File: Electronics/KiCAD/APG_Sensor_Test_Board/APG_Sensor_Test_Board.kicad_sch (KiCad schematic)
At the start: 0 parts

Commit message: Main Schematic Complete
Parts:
- added J2: Conn_01x02, symbol Connector_Generic:Conn_01x02
- added J3, J6: Conn_01x05, symbol Connector_Generic:Conn_01x05
- added J5: Conn_01x03, symbol Connector_Generic:Conn_01x03
- added R17, R18: 10k, symbol Device:R
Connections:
- net Baro/SCLK: now also R17.2
- net ESP32/IO1: now also J3.1 (Pin_1)
- net ESP32/IO10: now also J3.5 (Pin_5)
- net ESP32/IO18: now also J6.1 (Pin_1)
- net ESP32/IO2: now also J3.2 (Pin_2)
- net ESP32/IO38: now also J6.2 (Pin_2)
- net ESP32/IO39: now also J6.3 (Pin_3)
- net ESP32/IO40: now also J6.4 (Pin_4)
- net ESP32/IO41: now also J6.5 (Pin_5)
- net ESP32/IO42: now also J5.1 (Pin_1)
- net ESP32/IO8: now also J3.3 (Pin_3)
- net ESP32/IO9: now also J3.4 (Pin_4)
- net ESP32/RX: now also J5.2 (Pin_2)
- net ESP32/TX: now also J5.3 (Pin_3)
- new net +3V3: R17.1, R18.1
- new net ADC1: J2.2 (Pin_2)
- new net Baro/SDA: R18.2
- new net GND: J2.1 (Pin_1)
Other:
- sheet Baro ports: added SDA; removed CSB, SDI, SDO
- sheet High_G_Accel ports: added SDA; removed SDI, SDO, nCS
- sheet IMU ports: added BNO_BOOTN, BNO_NRST, H_INTN, H_SCL, H_SDA; removed none

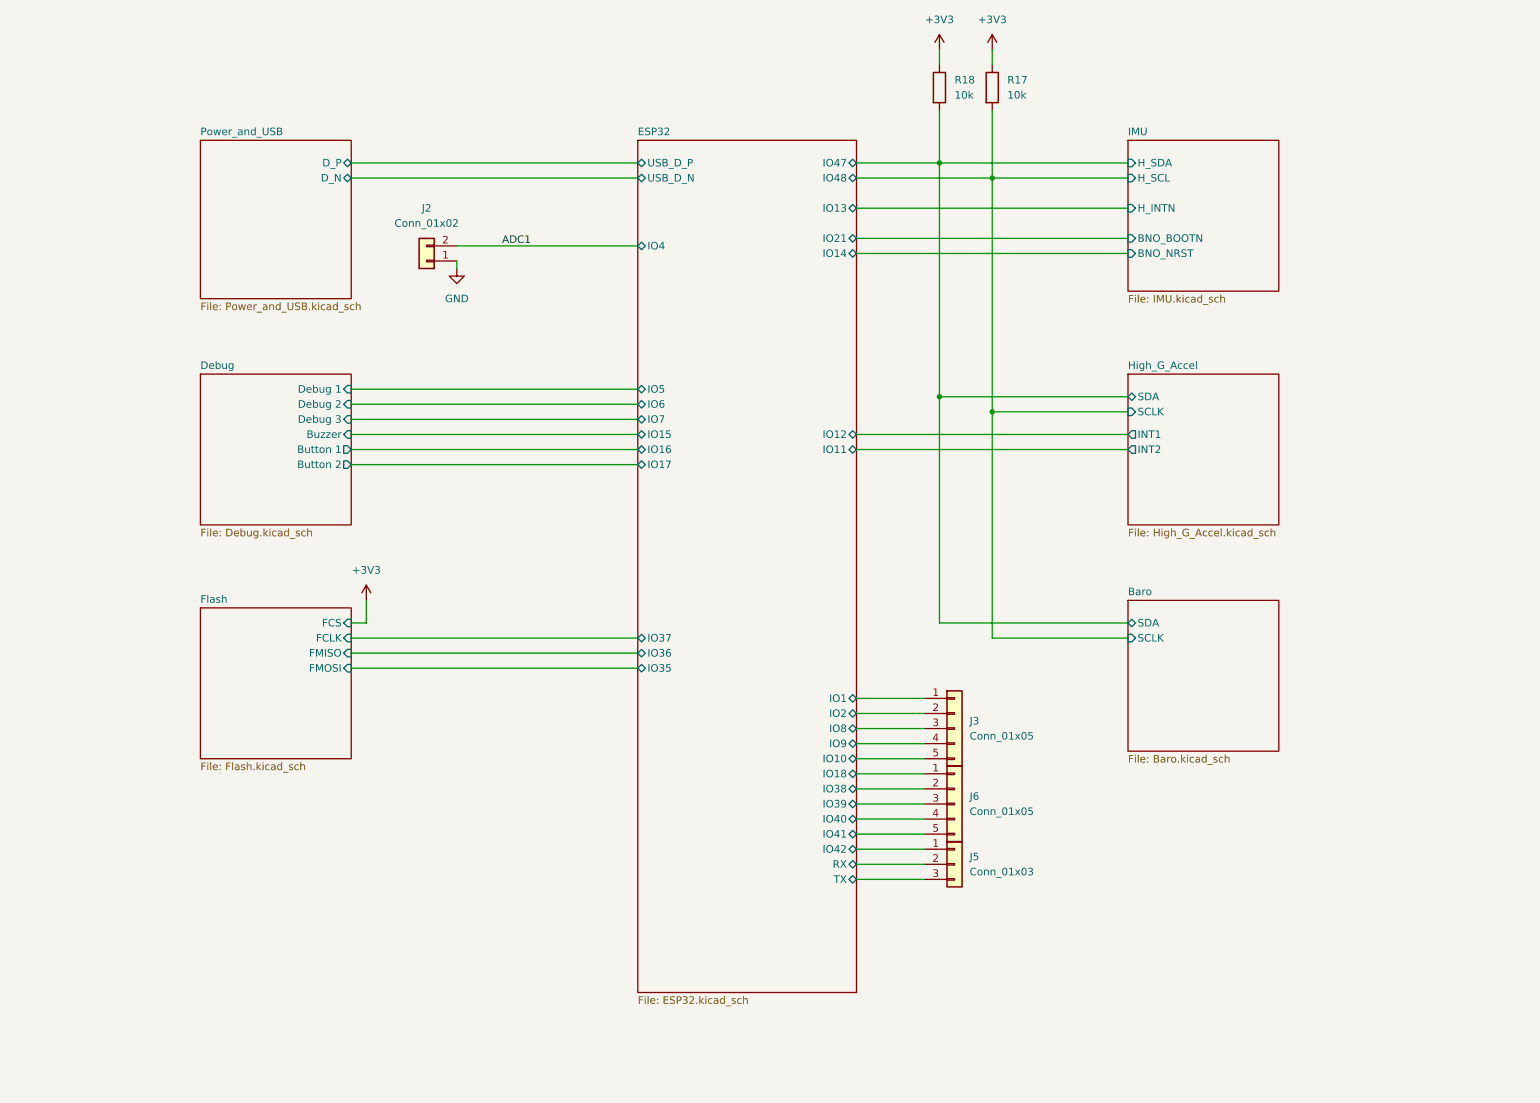
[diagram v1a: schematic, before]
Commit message: reaninotate and begin footprints
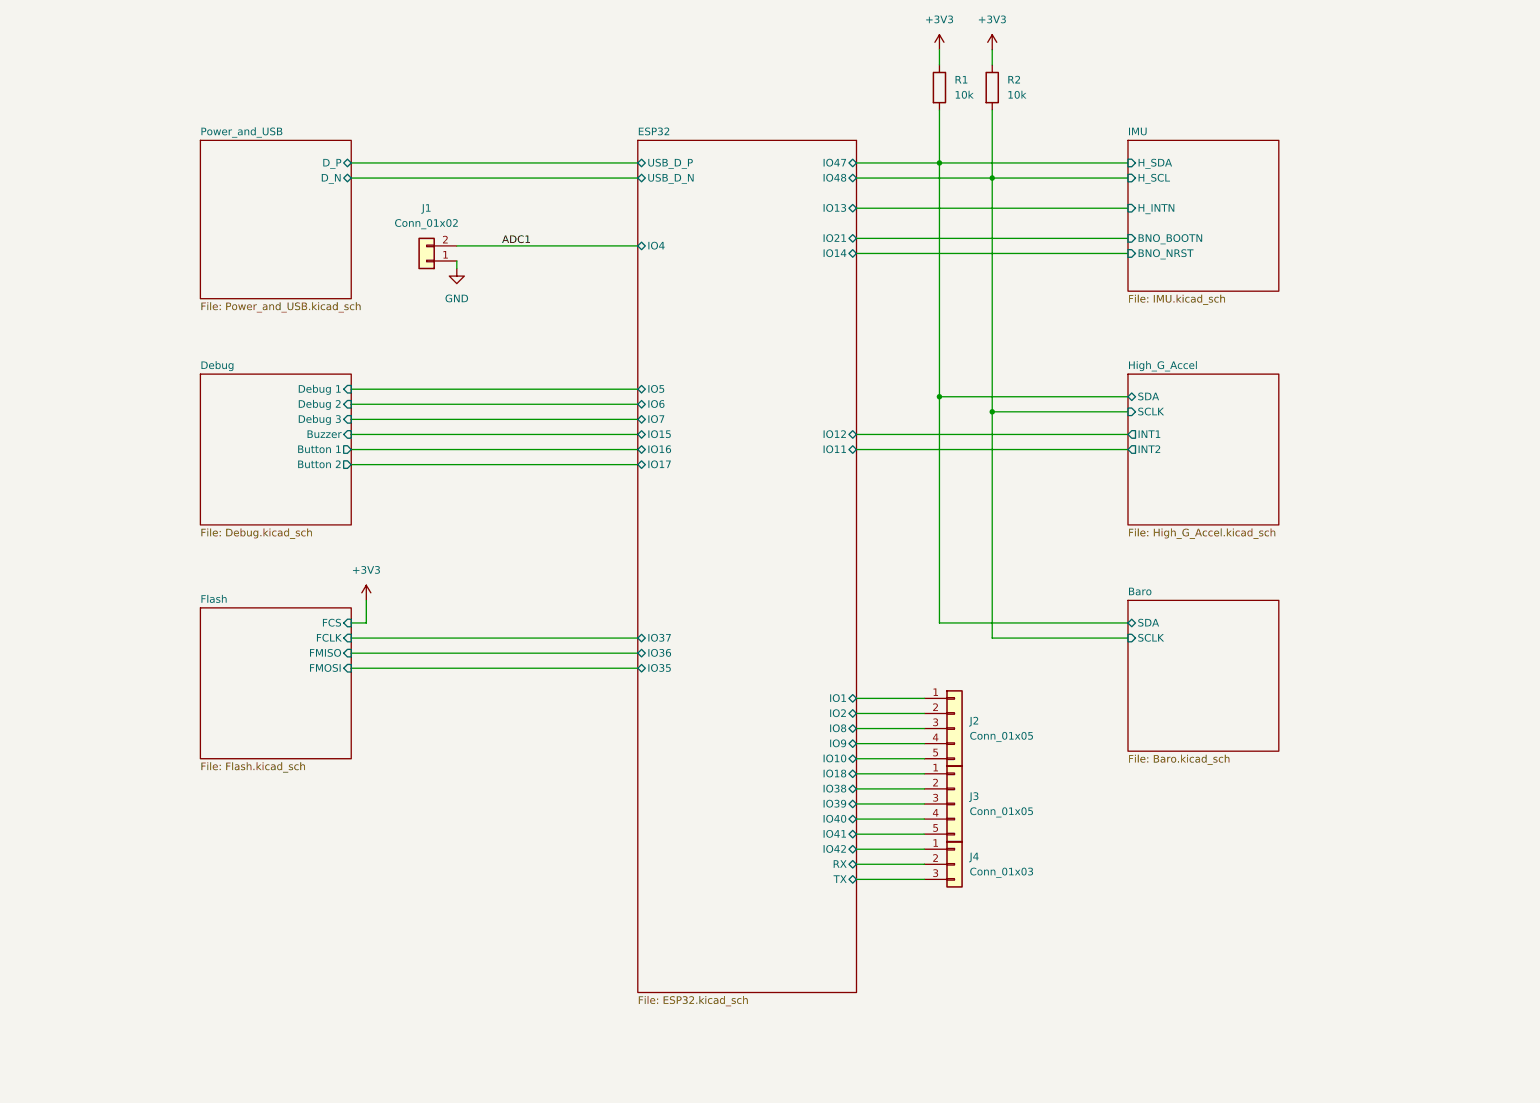
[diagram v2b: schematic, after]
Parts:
- J1: renamed from J2; footprint (none) -> Connector_PinHeader_2.54mm:PinHeader_1x02_P2.54mm_Vertical
- J2: renamed from J3; footprint (none) -> Connector_PinHeader_2.54mm:PinHeader_1x05_P2.54mm_Vertical
- J3: renamed from J6; footprint (none) -> Connector_PinHeader_2.54mm:PinHeader_1x05_P2.54mm_Vertical
- J4: renamed from J5; footprint (none) -> Connector_PinHeader_2.54mm:PinHeader_1x03_P2.54mm_Vertical
- R1: renamed from R18; footprint (none) -> Resistor_SMD:R_0805_2012Metric
- R2: renamed from R17; footprint (none) -> Resistor_SMD:R_0805_2012Metric
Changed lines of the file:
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@@
 		(dnp no)
 		(fields_autoplaced yes)
-		(property "Reference" "J3"
+		(property "Reference" "J2"
 			(at 176.53 134.6199 0)
 			(effects
@@
 			)
 		)
-		(property "Footprint" ""
+		(property "Footprint" "Connector_PinHeader_2.54mm:PinHeader_1x05_P2.54mm_Vertical"
 			(at 173.99 135.89 0)
 			(effects
@@
 			(project ""
 				(path "/3161be0c-372f-463d-be0a-bab00f344057"
-					(reference "J3")
+					(reference "J2")
 					(unit 1)
 				)
@@
 		(dnp no)
 		(fields_autoplaced yes)
-		(property "Reference" "R18"
+		(property "Reference" "R1"
 			(at 173.99 26.6699 0)
 			(effects
@@
 			)
 		)
-		(property "Footprint" ""
+		(property "Footprint" "Resistor_SMD:R_0805_2012Metric"
 			(at 169.672 27.94 90)
 			(effects
@@
 			(project ""
 				(path "/3161be0c-372f-463d-be0a-bab00f344057"
-					(reference "R18")
+					(reference "R1")
 					(unit 1)
 				)
@@
 		(dnp no)
 		(fields_autoplaced yes)
-		(property "Reference" "J2"
+		(property "Reference" "J1"
 			(at 85.09 48.26 0)
 			(effects
@@
 			)
 		)
-		(property "Footprint" ""
+		(property "Footprint" "Connector_PinHeader_2.54mm:PinHeader_1x02_P2.54mm_Vertical"
 			(at 85.09 57.15 0)
 			(effects
@@
 			(project ""
 				(path "/3161be0c-372f-463d-be0a-bab00f344057"
-					(reference "J2")
+					(reference "J1")
 					(unit 1)
 				)
@@
 		(dnp no)
 		(fields_autoplaced yes)
-		(property "Reference" "#PWR048"
+		(property "Reference" "#PWR04"
 			(at 180.34 25.4 0)
 			(effects
@@
 			(project "APG_Sensor_Test_Board"
 				(path "/3161be0c-372f-463d-be0a-bab00f344057"
-					(reference "#PWR048")
+					(reference "#PWR04")
 					(unit 1)
 				)
@@
 		(dnp no)
 		(fields_autoplaced yes)
-		(property "Reference" "J6"
+		(property "Reference" "J3"
 			(at 176.53 147.3199 0)
 			(effects
@@
 			)
 		)
-		(property "Footprint" ""
+		(property "Footprint" "Connector_PinHeader_2.54mm:PinHeader_1x05_P2.54mm_Vertical"
 			(at 173.99 148.59 0)
 			(effects
@@
 			(project "APG_Sensor_Test_Board"
 				(path "/3161be0c-372f-463d-be0a-bab00f344057"
-					(reference "J6")
+					(reference "J3")
 					(unit 1)
 				)
@@
 		(dnp no)
 		(fields_autoplaced yes)
-		(property "Reference" "#PWR050"
+		(property "Reference" "#PWR02"
 			(at 90.17 64.77 0)
 			(effects
@@
 			(project ""
 				(path "/3161be0c-372f-463d-be0a-bab00f344057"
-					(reference "#PWR050")
+					(reference "#PWR02")
 					(unit 1)
 				)
@@
 		(dnp no)
 		(fields_autoplaced yes)
-		(property "Reference" "R17"
+		(property "Reference" "R2"
 			(at 182.88 26.6699 0)
 			(effects
@@
 			)
 		)
-		(property "Footprint" ""
+		(property "Footprint" "Resistor_SMD:R_0805_2012Metric"
 			(at 178.562 27.94 90)
 			(effects
@@
 			(project ""
 				(path "/3161be0c-372f-463d-be0a-bab00f344057"
-					(reference "R17")
+					(reference "R2")
 					(unit 1)
 				)
@@
 		(dnp no)
 		(fields_autoplaced yes)
-		(property "Reference" "#PWR051"
+		(property "Reference" "#PWR01"
 			(at 74.93 118.11 0)
 			(effects
@@
 			(project "APG_Sensor_Test_Board"
 				(path "/3161be0c-372f-463d-be0a-bab00f344057"
-					(reference "#PWR051")
+					(reference "#PWR01")
 					(unit 1)
 				)
@@
 		(dnp no)
 		(fields_autoplaced yes)
-		(property "Reference" "J5"
+		(property "Reference" "J4"
 			(at 176.53 157.4799 0)
 			(effects
@@
 			)
 		)
-		(property "Footprint" ""
+		(property "Footprint" "Connector_PinHeader_2.54mm:PinHeader_1x03_P2.54mm_Vertical"
 			(at 173.99 158.75 0)
 			(effects
@@
 			(project ""
 				(path "/3161be0c-372f-463d-be0a-bab00f344057"
-					(reference "J5")
+					(reference "J4")
 					(unit 1)
 				)
@@
 		(dnp no)
 		(fields_autoplaced yes)
-		(property "Reference" "#PWR047"
+		(property "Reference" "#PWR03"
 			(at 171.45 25.4 0)
 			(effects
@@
 			(project "APG_Sensor_Test_Board"
 				(path "/3161be0c-372f-463d-be0a-bab00f344057"
-					(reference "#PWR047")
-					(unit 1)
-				)
+					(reference "#PWR03")
+					(unit 1)
+				)

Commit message: added test points
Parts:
- added TP1: SDA, symbol Connector:TestPoint
- added TP2: SCL, symbol Connector:TestPoint
- added TP3: FCLK, symbol Connector:TestPoint
- added TP4: FMISO, symbol Connector:TestPoint
- added TP5: FMOSI, symbol Connector:TestPoint
- added TP8: D_P, symbol Connector:TestPoint
- added TP9: D_N, symbol Connector:TestPoint
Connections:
- net Baro/SCLK: now also TP2.1
- net Baro/SDA: now also TP1.1
- net ESP32/IO35: now also TP5.1
- net ESP32/IO36: now also TP4.1
- net ESP32/IO37: now also TP3.1
- net ESP32/USB_D_N: now also TP9.1
- net ESP32/USB_D_P: now also TP8.1
